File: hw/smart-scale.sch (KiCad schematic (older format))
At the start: 29 parts

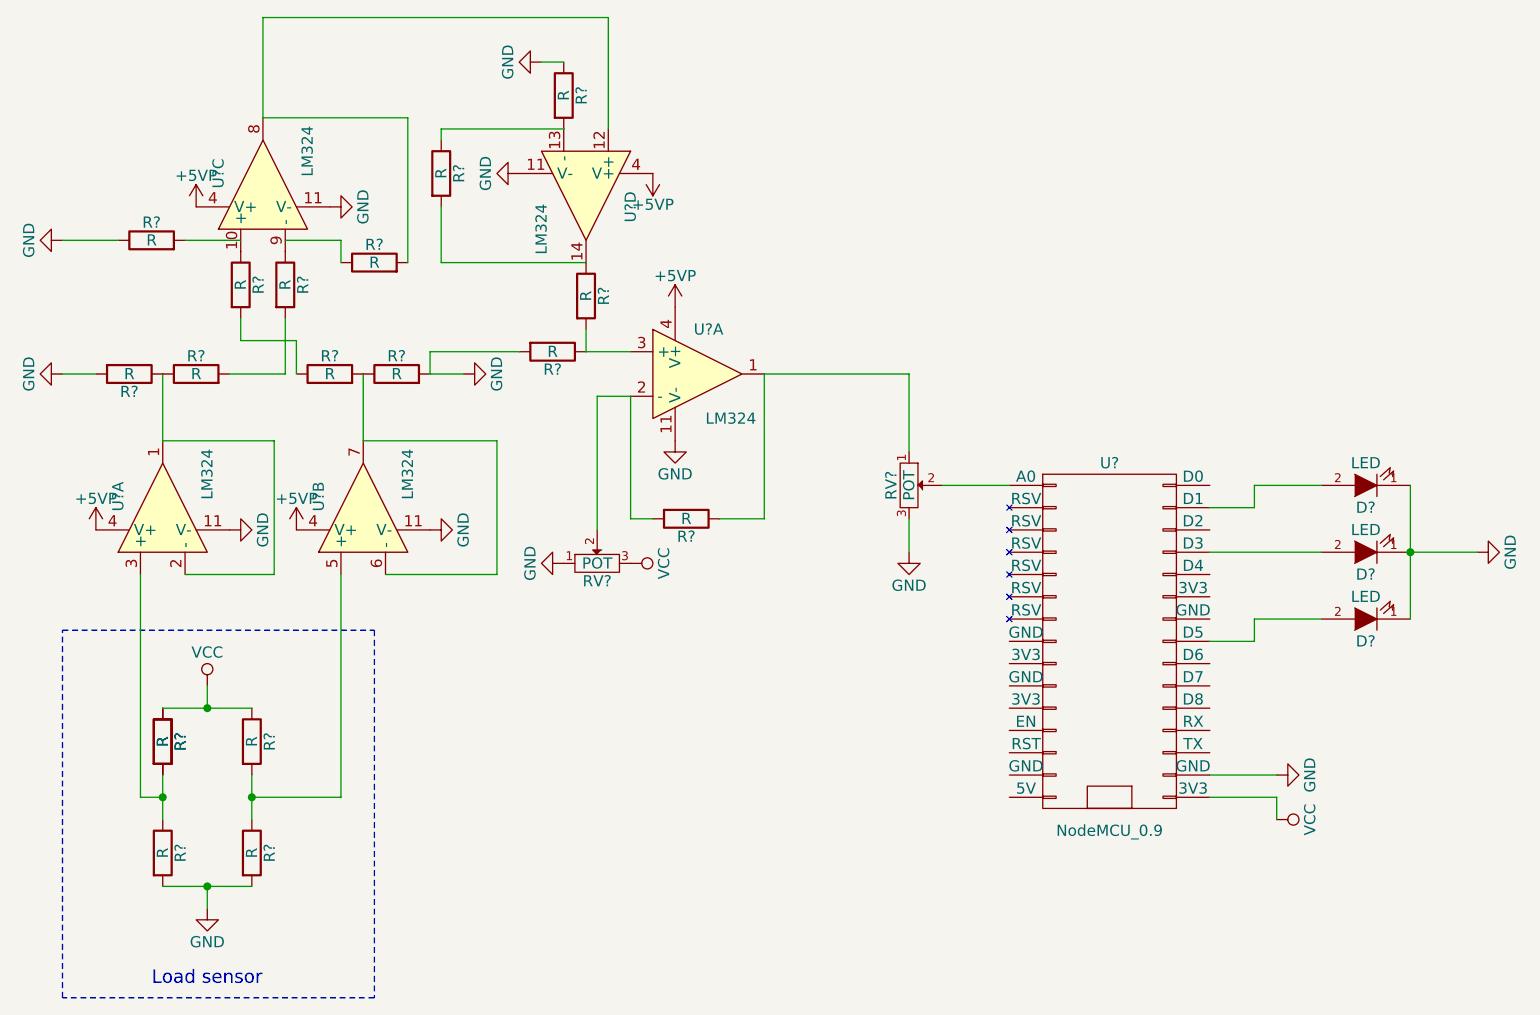
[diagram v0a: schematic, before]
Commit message: Added resistor values
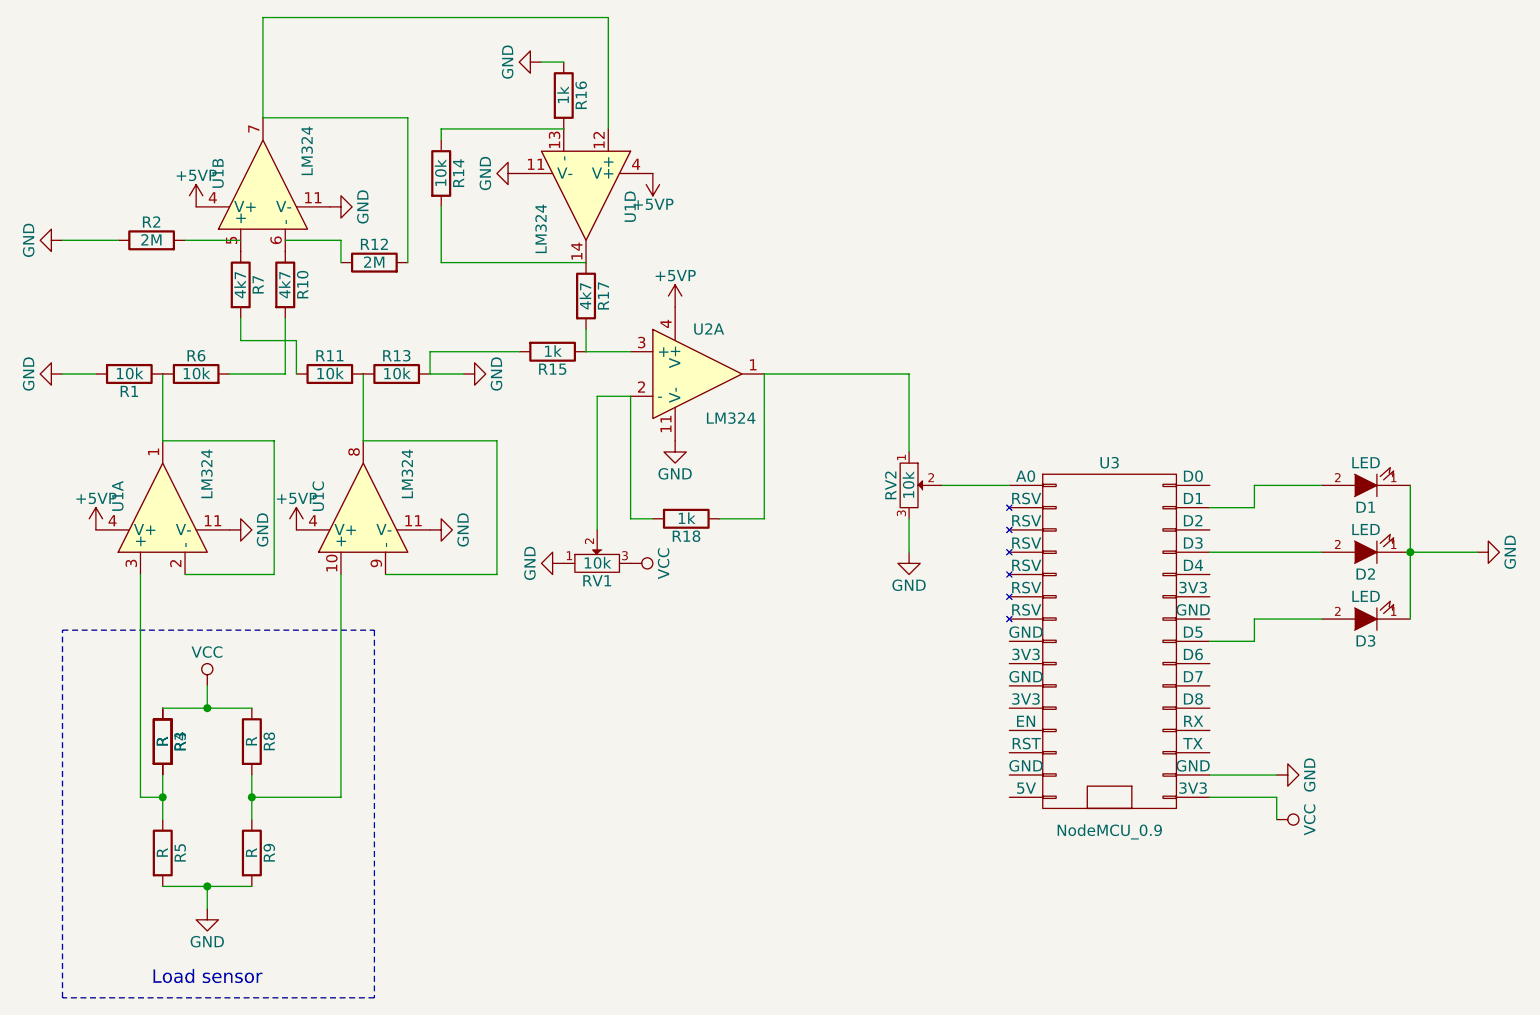
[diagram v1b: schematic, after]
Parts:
- R1, R11, R13, R14, R6: renamed from R?; value R -> 10k
- R10, R17, R7: renamed from R?; value R -> 4k7
- R12, R2: renamed from R?; value R -> 2M
- R15, R16, R18: renamed from R?; value R -> 1k
- RV1, RV2: renamed from RV?; value POT -> 10k
- gave numbers to parts that had none: 11
